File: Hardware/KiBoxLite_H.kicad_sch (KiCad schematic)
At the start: 151 parts, among them J1 Screw_Terminal_01x03, J2 USB4105-GF-A-060, Q2 BC817-40(SOT23), Q3 BC817-40(SOT23), T1 LMUN2211LT1G(SOT-23), U1 CH340X(MSOP-10), U10 MAX13487, U3 TP4054-42-SOT25-R(SOT23-5), U4 LAN8710A-EZC(QFN32), U5 TX4138(ESOIC-8), U6 ESP32-WROOM-32E-N4, U7 TPS62A02ADRLR(SOT-563-6), U8 NA(SN74LVC1G04DBVR(SOT23-5)), U9 TPS2378DDAR(HSOIC-8)

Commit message: build: TestPoint logo
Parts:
- added TP_3.3V1, TP_485A1, TP_485B1, TP_485TX1, TP_EN1, TP_GND1, TP_MDC1, TP_MDIO1, TP_PoE_OUT1, TP_VBAT1, TP_VBUS1: TestPoint, TestPoint:TestPoint_Pad_1.0x1.0mm, symbol Connector:TestPoint
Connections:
- net +3.3V: now also TP_3.3V1.1
- net ESP_EN: now also TP_EN1.1
- net GND: now also TP_GND1.1
- net GPIO18\MDIO(RMII): now also TP_MDIO1.1
- net GPIO23\MDC(RMII): now also TP_MDC1.1
- net VBUS: now also TP_VBUS1.1
- net VBAT: now reaches BAT1.1, FET2.3, R17.1, U3.3 (VBAT)
- net VBAT: now also TP_VBAT1.1
- net PoE_OUT: now reaches C12.1, D5.1 (K), L4.1, R43.2, U5.1 (SW)
- net PoE_OUT: now also TP_PoE_OUT1.1
- net 485_B: now reaches D4.1 (A1), F1.1, R31.2, R36.1, U10.7 (B)
- net 485_B: now also TP_485B1.1
- net 485_A: now reaches D4.2 (A2), F2.1, JP1.1 (A), R35.1, U10.6 (A)
- net 485_A: now also TP_485A1.1
- net GPIO4\U1TXD renamed 485_TX
- net 485_TX: now also TP_485TX1.1
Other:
- note added: "Alimentación"
- note added: "Control"
- note added: "Validations Points"
- moved on the sheet: C12, C23, C24, C25, C26, C27, Class4_EN1, D10, D11, D4, D5, D8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

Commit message: build: .step
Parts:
- removed TP_MDC1, TP_MDIO1: TestPoint, TestPoint:TestPoint_Pad_1.0x1.0mm, symbol Connector:TestPoint
- added TP_485POE1, TP_485RX1: TestPoint, TestPoint:TestPoint_Pad_1.0x1.0mm, symbol Connector:TestPoint
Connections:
- net +5V: now also TP_485POE1.1
- net GPI36\U1RXD renamed 485_RX
- net 485_RX: now also TP_485RX1.1

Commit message: build: fuse ts250
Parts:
- F1, F2: footprint Fuse:Fuse_1206_3216Metric -> kiboard_shield:TS250
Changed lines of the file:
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@@
 			)
 		)
-		(property "Footprint" "Fuse:Fuse_1206_3216Metric"
+		(property "Footprint" "kiboard_shield:TS250"
 			(at 394.97 267.97 0)
 			(hide yes)
@@
 			)
 		)
-		(property "Footprint" "Fuse:Fuse_1206_3216Metric"
+		(property "Footprint" "kiboard_shield:TS250"
 			(at 398.78 243.84 0)
 			(hide yes)

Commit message: build: Cambio de puerto rs485
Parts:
- J1: footprint TerminalBlock_Phoenix:TerminalBlock_Phoenix_MKDS-1,5-3-5.08_1x03_P5.08mm_Horizontal -> Connector_Phoenix_MSTB:PhoenixContact_MSTBA_2,5_3-G_1x03_P5.00mm_Horizontal
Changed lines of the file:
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@@
 			)
 		)
-		(property "Footprint" "TerminalBlock_Phoenix:TerminalBlock_Phoenix_MKDS-1,5-3-5.08_1x03_P5.08mm_Horizontal"
+		(property "Footprint" "Connector_Phoenix_MSTB:PhoenixContact_MSTBA_2,5_3-G_1x03_P5.00mm_Horizontal"
 			(at 406.4 252.73 0)
 			(hide yes)
@@
 			(at 406.4 252.73 0)
 			(hide yes)
+			(show_name no)
+			(do_not_autoplace no)
+			(effects
+				(font
+					(size 1.27 1.27)
+				)
+			)
+		)
+		(property "Value IND" ""
+			(at 406.4 252.73 0)
+			(hide yes)
+			(show_name no)
+			(do_not_autoplace no)
+			(effects
+				(font
+					(size 1.27 1.27)
+				)
+			)
+		)
+		(property "Value 16MB" ""
+			(at 406.4 252.73 0)
+			(hide yes)
+			(show_name no)
+			(do_not_autoplace no)
+			(effects
+				(font
+					(size 1.27 1.27)
+				)
+			)
+		)
+		(property "Value EA" ""
+			(at 406.4 252.73 0)
+			(hide yes)
+			(show_name no)
+			(do_not_autoplace no)
+			(effects
+				(font
+					(size 1.27 1.27)
+				)
+			)
+		)
+		(property "Value EA-IND" ""
+			(at 406.4 252.73 0)
+			(hide yes)
+			(show_name no)
+			(do_not_autoplace no)
+			(effects
+				(font
+					(size 1.27 1.27)
+				)
+			)
+		)
+		(property "Value EA-16MB" ""
+			(at 406.4 252.73 0)
+			(hide yes)
+			(show_name no)
+			(do_not_autoplace no)
+			(effects
+				(font
+					(size 1.27 1.27)
+				)
+			)
+		)
+		(property "Value WROVER" ""
+			(at 406.4 252.73 0)
+			(hide yes)
+			(show_name no)
+			(do_not_autoplace no)
+			(effects
+				(font
+					(size 1.27 1.27)
+				)
+			)
+		)
+		(property "Value WROVER-EA" ""
+			(at 406.4 252.73 0)
+			(hide yes)

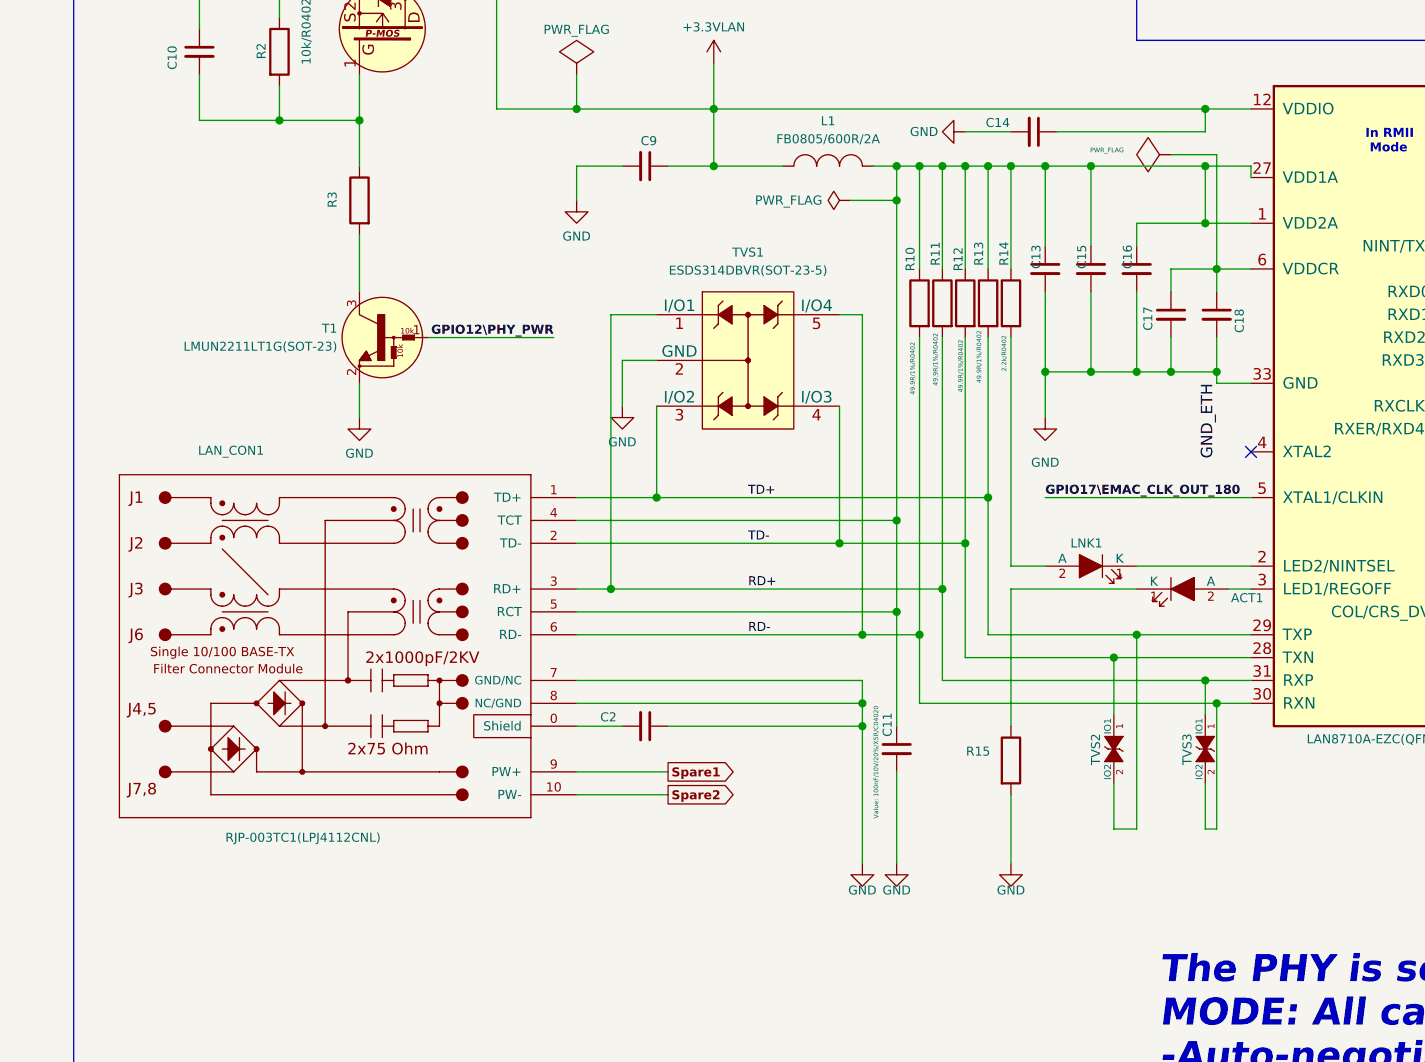
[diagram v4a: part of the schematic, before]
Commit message: build: rj45 con leds
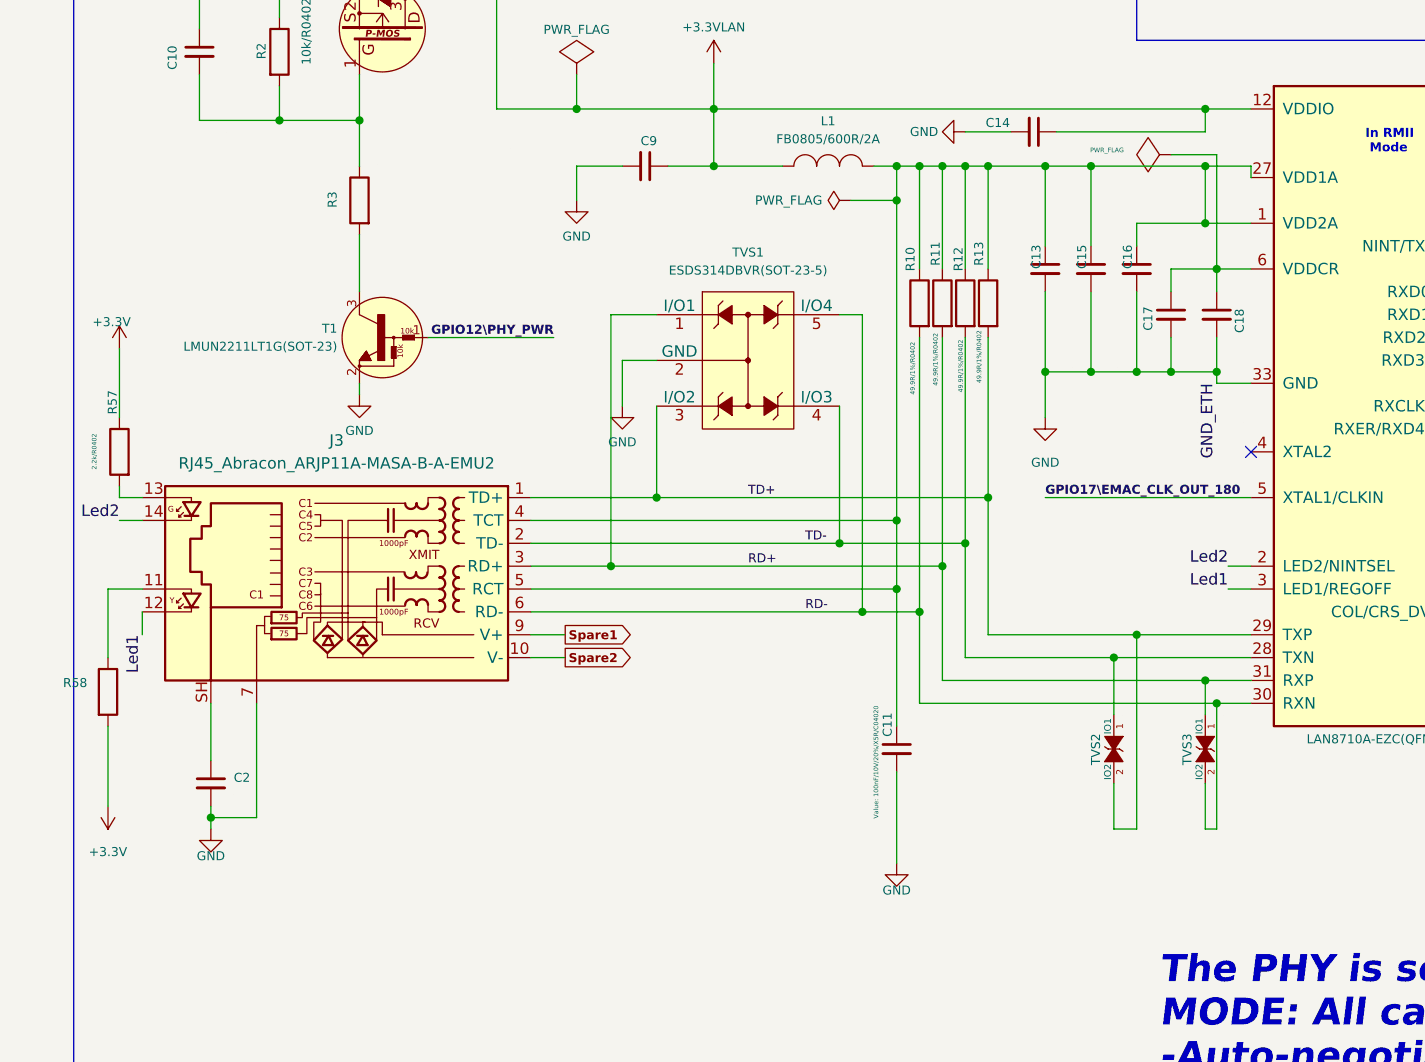
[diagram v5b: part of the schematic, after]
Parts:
- removed ACT1: LED/YELLOW/0603, OLIMEX_LEDs-FP:LED_0603_KA, symbol OLIMEX_Diodes:LED
- removed LAN_CON1: RJP-003TC1(LPJ4112CNL), OLIMEX_Connectors-FP:RJP-003TC1(LPJ4112CNL), symbol OLIMEX_Connectors:RJP-003TC1(LPJ4112CNL)
- removed LNK1: LED/GREEN/0603, OLIMEX_LEDs-FP:LED_0603_KA, symbol OLIMEX_Diodes:LED
- removed R14, R15: 2.2k/R0402, OLIMEX_RLC-FP:R_0402_5MIL_DWS, symbol OLIMEX_RCL:R
- added J3: RJ45_Abracon_ARJP11A-MASA-B-A-EMU2, Connector_RJ:RJ45_Abracon_ARJP11A-MA_Horizontal, symbol Connector:RJ45_Abracon_ARJP11A-MASA-B-A-EMU2
- added R57, R58: 2.2k/R0402, OLIMEX_RLC-FP:R_0402_5MIL_DWS, symbol OLIMEX_RCL:R
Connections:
- net +3.3V: now also R57.1, R58.2
- net GND: now also C2.2, J3.7; no longer C2.1
- net RD+: now also J3.3 (RD+)
- net RD-: now also J3.6 (RD-)
- net Spare1: now also J3.9 (V+)
- net Spare2: now also J3.10 (V-)
- net TD+: now also J3.1 (TD+)
- net TD-: now also J3.2 (TD-)
- net at C11.1, C13.1, C15.1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: now also J3.4 (TCT), J3.5 (RCT)
- net Led2: now reaches U4.2 (LED2/NINTSEL)
- net Led2: now also J3.14
- net Led1: now reaches U4.3 (LED1/REGOFF)
- net Led1: now also J3.12
- new net: C2.1, J3.SH
- new net: J3.11, R58.1
- new net: J3.13, R57.2
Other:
- moved on the sheet: C2

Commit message: build: optimizacion pcb
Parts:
- renumbered TP_3.3V1 to 3.3V1, TP_485A1 to 485A1, TP_485B1 to 485B1, TP_485POE1 to 485POE1, TP_485RX1 to 485RX1, TP_485TX1 to 485TX1, TP_EN1 to EN1, TP_GND1 to GND1, TP_PoE_OUT1 to PoE1, TP_VBAT1 to VBAT1, TP_VBUS1 to VBUS1
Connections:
- net +5V: now also EXT2.7; no longer EXT1.1
- net GPIO16\I2C-SCL: now also EXT1.1; no longer EXT2.7
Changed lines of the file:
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@@
 	)
 	(bus_entry
-		(at 572.77 185.42)
-		(size 2.54 -2.54)
-		(stroke
-			(width 0)
-			(type default)
-		)
-	)
-	(bus_entry
 		(at 463.55 184.15)
 		(size 2.54 2.54)
@@
 	)
 	(bus_entry
+		(at 463.55 168.91)
+		(size 2.54 2.54)
+		(stroke
+			(width 0)
+			(type default)
+		)
+	)
+	(bus_entry
 		(at 436.88 46.99)
 		(size 2.54 -2.54)
@@
 	(wire
 		(pts
+			(xy 466.09 171.45) (xy 500.38 171.45)
+		)
+		(stroke
+			(width 0)
+			(type default)
+		)
+	)
+	(wire
+		(pts
 			(xy 72.39 166.37) (xy 72.39 170.18)
 		)
@@
 	(wire
 		(pts
-			(xy 546.1 185.42) (xy 572.77 185.42)
-		)
-		(stroke
-			(width 0)
-			(type default)
-		)
-	)
-	(wire
-		(pts
 			(xy 289.56 46.99) (xy 292.1 46.99)
 		)
@@
 	(bus
 		(pts
-			(xy 575.31 182.88) (xy 575.31 185.42)
+			(xy 575.31 180.34) (xy 575.31 185.42)
 		)
 		(stroke
@@
 		)
 	)
-	(bus
-		(pts
-			(xy 575.31 180.34) (xy 575.31 182.88)
-		)
-		(stroke
-			(width 0)
-			(type default)
-		)
-	)
 	(wire
 		(pts
@@
 	(wire
 		(pts
-			(xy 483.87 171.45) (xy 500.38 171.45)
-		)
-		(stroke
-			(width 0)
-			(type default)
-		)
-	)
-	(wire
-		(pts
 			(xy 396.24 39.37) (xy 391.16 39.37)
 		)
@@
 	)
 	(label "GPIO16\\I2C-SCL"
-		(at 553.72 185.42 0)
+		(at 480.06 171.45 0)
 		(effects
 			(font
@@
 	(symbol
 		(lib_id "OLIMEX_Power:+5V")
-		(at 483.87 171.45 90)
+		(at 546.1 185.42 270)
 		(unit 1)
 		(body_style 1)
@@
 		(fields_autoplaced yes)
 		(property "Reference" "#PWR067"
-			(at 487.87 171.45 0)
+			(at 542.1 185.42 0)
 			(hide yes)
 			(show_name no)
@@
 		)
 		(property "Value" "+5V"
-			(at 480.87 170.45 90)
+			(at 549.91 185.42 90)
 			(show_name no)
 			(do_not_autoplace no)
@@
 		)
 		(property "Footprint" ""
-			(at 483.87 171.45 0)
+			(at 546.1 185.42 0)
 			(show_name no)
 			(do_not_autoplace no)
@@
 		)
 		(property "Datasheet" ""
-			(at 483.87 171.45 0)
+			(at 546.1 185.42 0)
 			(show_name no)
 			(do_not_autoplace no)
@@
 		)
 		(property "Description" ""
-			(at 483.87 171.45 0)
+			(at 546.1 185.42 0)
 			(show_name no)
 			(do_not_autoplace no)
@@
 		(dnp no)
 		(fields_autoplaced yes)
-		(property "Reference" "TP_485A1"
+		(property "Reference" "485A1"
 			(at 527.05 240.0299 90)
 			(show_name no)
@@
 			(project "KiBoxLite_H"
 				(path "/b90747b7-8201-400d-ac9b-e7137fd496cd"
-					(reference "TP_485A1")
+					(reference "485A1")
 					(unit 1)
 				)
@@
 		(dnp no)
 		(fields_autoplaced yes)
-		(property "Reference" "TP_GND1"
+		(property "Reference" "GND1"
 			(at 482.6 265.4299 90)
 			(show_name no)
@@
 			(project "KiBoxLite_H"
 				(path "/b90747b7-8201-400d-ac9b-e7137fd496cd"
-					(reference "TP_GND1")
+					(reference "GND1")
 					(unit 1)
 				)
@@
 		(dnp no)
 		(fields_autoplaced yes)
-		(property "Reference" "TP_485TX1"
+		(property "Reference" "485TX1"
 			(at 527.05 252.7299 90)
 			(show_name no)
@@
 			(project "KiBoxLite_H"
 				(path "/b90747b7-8201-400d-ac9b-e7137fd496cd"
-					(reference "TP_485TX1")
+					(reference "485TX1")
 					(unit 1)
 				)
@@
 		(dnp no)
 		(fields_autoplaced yes)
-		(property "Reference" "TP_3.3V1"
+		(property "Reference" "3.3V1"
 			(at 482.6 246.3799 90)
 			(show_name no)
@@
 			(project "KiBoxLite_H"
 				(path "/b90747b7-8201-400d-ac9b-e7137fd496cd"
-					(reference "TP_3.3V1")
+					(reference "3.3V1")
 					(unit 1)
 				)
@@
 		(dnp no)
 		(fields_autoplaced yes)
-		(property "Reference" "TP_485RX1"
+		(property "Reference" "485RX1"
 			(at 527.05 259.0799 90)
 			(show_name no)
@@
 			(project "KiBoxLite_H"
 				(path "/b90747b7-8201-400d-ac9b-e7137fd496cd"
-					(reference "TP_485RX1")
+					(reference "485RX1")
 					(unit 1)
 				)
@@
 		(dnp no)
 		(fields_autoplaced yes)
-		(property "Reference" "TP_VBAT1"
+		(property "Reference" "VBAT1"
 			(at 482.6 259.0799 90)
 			(show_name no)
@@
 			(project "KiBoxLite_H"
 				(path "/b90747b7-8201-400d-ac9b-e7137fd496cd"
-					(reference "TP_VBAT1")
+					(reference "VBAT1")
 					(unit 1)
 				)
@@
 		(dnp no)
 		(fields_autoplaced yes)
-		(property "Reference" "TP_VBUS1"
+		(property "Reference" "VBUS1"
 			(at 482.6 240.0299 90)
 			(show_name no)
@@
 			(project "KiBoxLite_H"
 				(path "/b90747b7-8201-400d-ac9b-e7137fd496cd"
-					(reference "TP_VBUS1")
+					(reference "VBUS1")
 					(unit 1)
 				)
@@
 		(dnp no)
 		(fields_autoplaced yes)
-		(property "Reference" "TP_485B1"
+		(property "Reference" "485B1"
 			(at 527.05 246.3799 90)
 			(show_name no)
@@
 			(project "KiBoxLite_H"
 				(path "/b90747b7-8201-400d-ac9b-e7137fd496cd"
-					(reference "TP_485B1")
+					(reference "485B1")
 					(unit 1)
 				)
@@
 		(dnp no)
 		(fields_autoplaced yes)
-		(property "Reference" "TP_EN1"
+		(property "Reference" "EN1"
 			(at 523.24 274.3199 90)
 			(show_name no)
@@
 			(project "KiBoxLite_H"
 				(path "/b90747b7-8201-400d-ac9b-e7137fd496cd"
-					(reference "TP_EN1")
+					(reference "EN1")
 					(unit 1)
 				)
@@
 		(dnp no)
 		(fields_autoplaced yes)
-		(property "Reference" "TP_485POE1"
+		(property "Reference" "485POE1"
 			(at 556.26 240.0299 90)
 			(show_name no)
@@
 			(project "KiBoxLite_H"
 				(path "/b90747b7-8201-400d-ac9b-e7137fd496cd"
-					(reference "TP_485POE1")
+					(reference "485POE1")
 					(unit 1)
 				)
@@
 		(dnp no)
 		(fields_autoplaced yes)
-		(property "Reference" "TP_PoE_OUT1"
+		(property "Reference" "PoE1"
 			(at 482.6 252.7299 90)
 			(show_name no)
@@
 			(project "KiBoxLite_H"
 				(path "/b90747b7-8201-400d-ac9b-e7137fd496cd"
-					(reference "TP_PoE_OUT1")
+					(reference "PoE1")
 					(unit 1)
 				)
